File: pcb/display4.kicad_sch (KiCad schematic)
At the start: 20 parts, among them Q13 DMG2301L, Q14 DMG2301L, Q15 DMG2301L, Q16 DMG2301L, U5 TPIC6C596

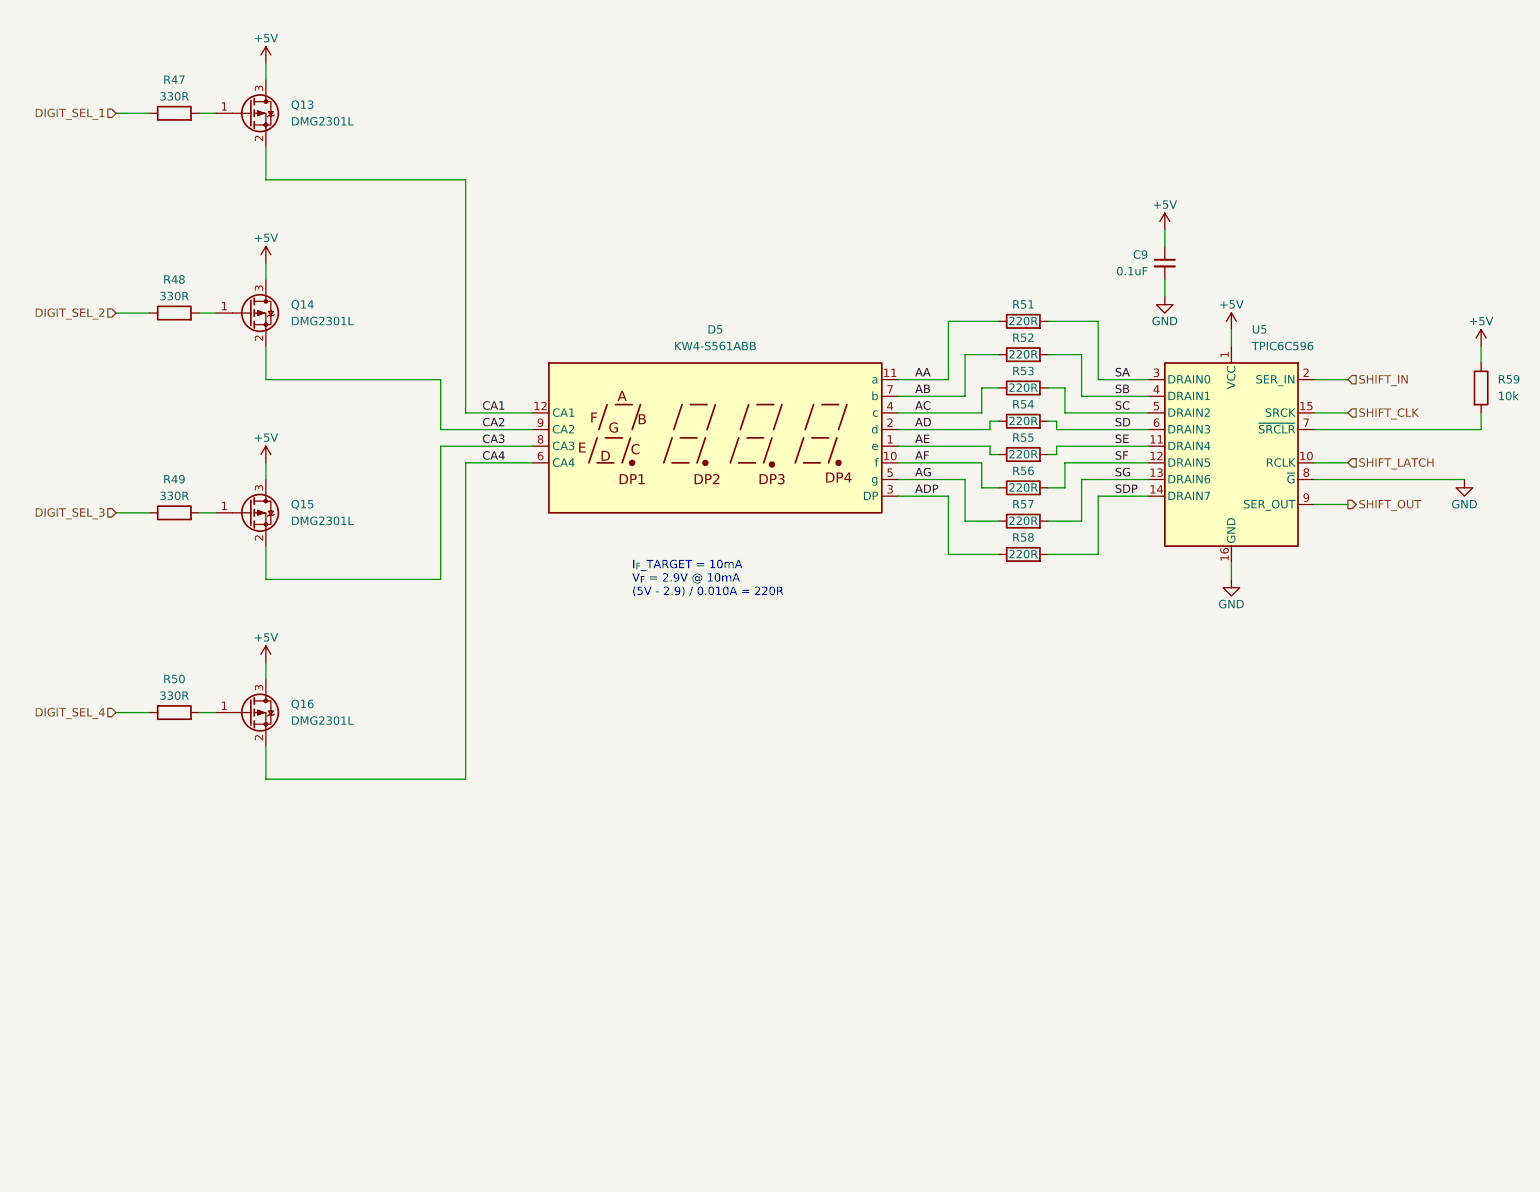
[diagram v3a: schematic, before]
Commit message: start to route display traces
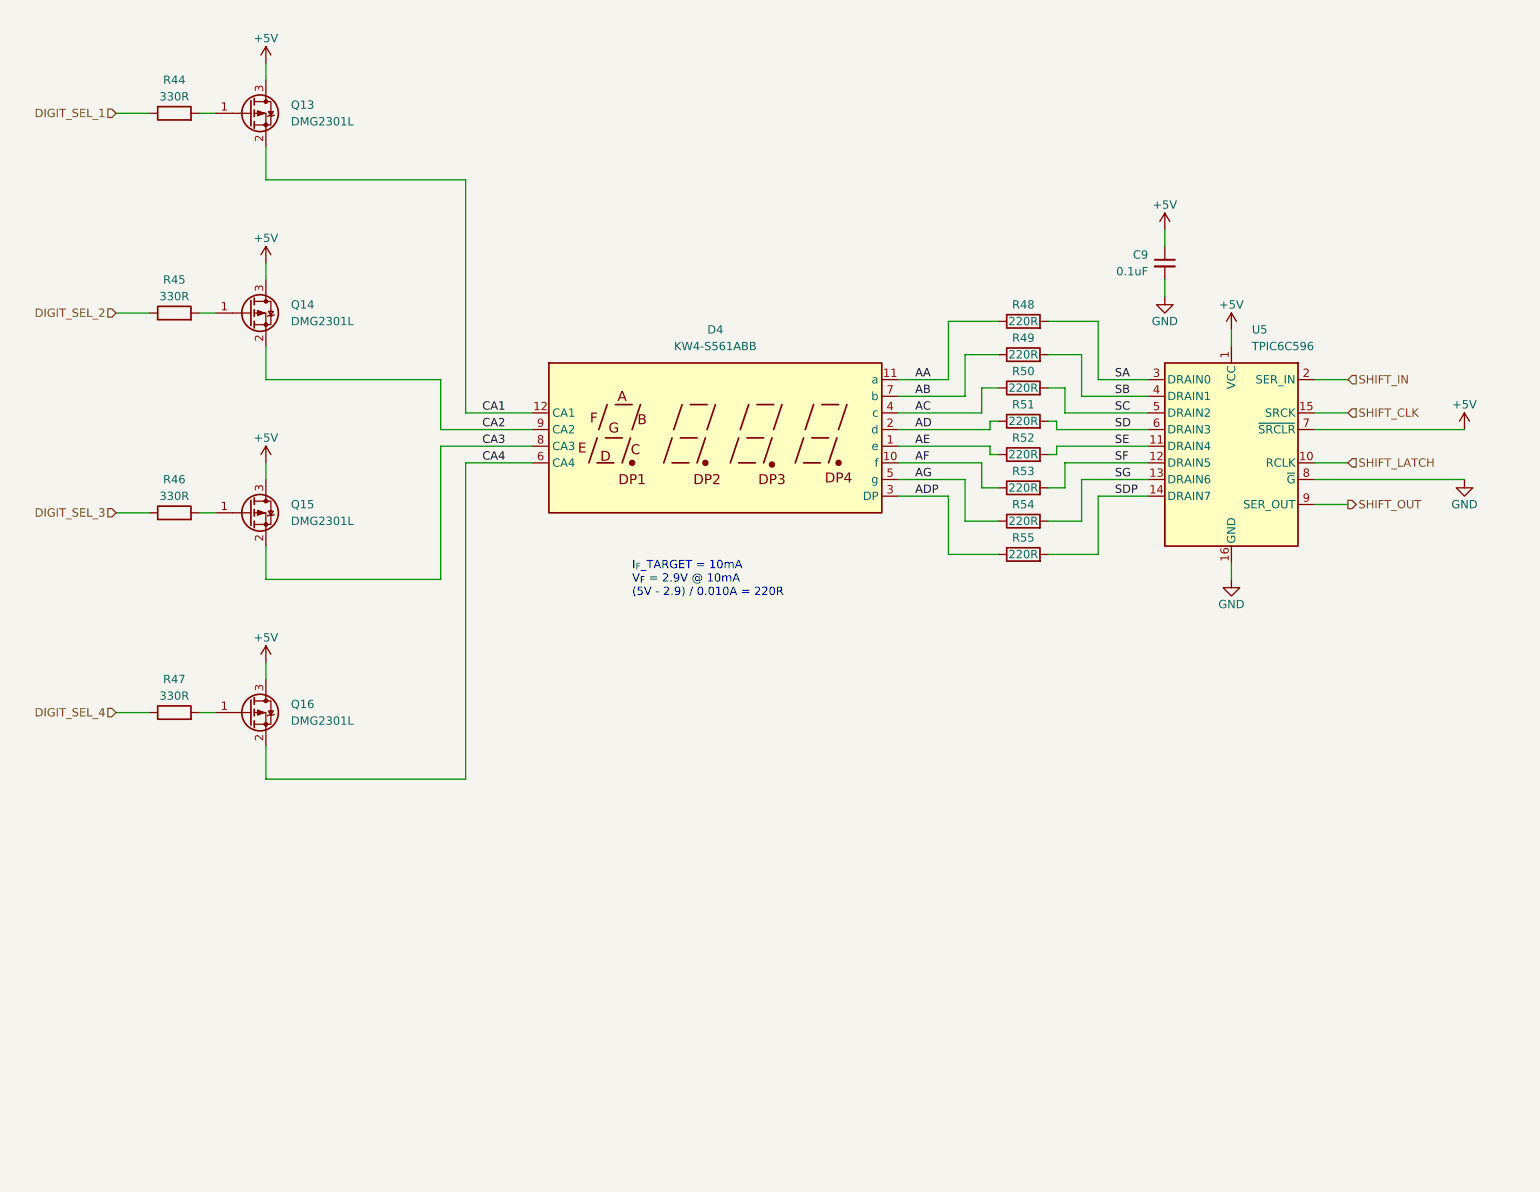
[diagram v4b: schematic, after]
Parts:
- removed R59: 10k, Resistor_SMD:R_0805_2012Metric_Pad1.20x1.40mm_HandSolder, symbol Device:R
- renumbered D5 to D4, R47 to R44, R48 to R45, R49 to R46, R50 to R47, R51 to R48, R52 to R49, R53 to R50, R54 to R51, R55 to R52, R56 to R53, R57 to R54, R58 to R55
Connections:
- net +5V: now also U5.7 (~{SRCLR})

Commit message: continue layout. improve 3d model
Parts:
- D4: footprint mtg_life_counter:KW4-S561xxB_SMD -> mtg_life_counter:KW4-S561xBB_SMD
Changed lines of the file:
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@@
 			)
 		)
-		(property "Footprint" "mtg_life_counter:KW4-S561xxB_SMD"
+		(property "Footprint" "mtg_life_counter:KW4-S561xBB_SMD"
 			(at 132.08 95.25 0)
 			(effects

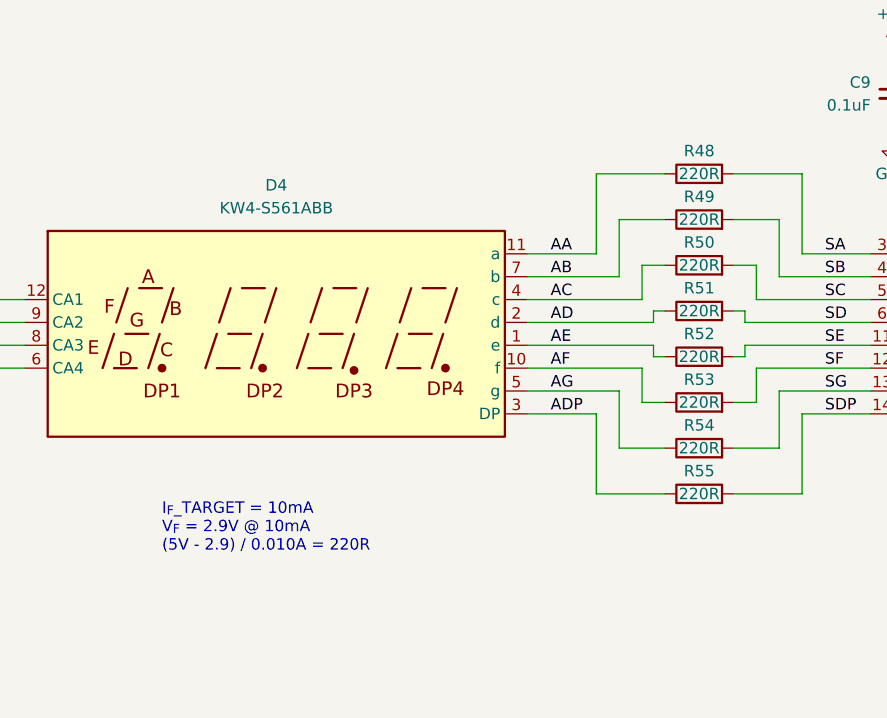
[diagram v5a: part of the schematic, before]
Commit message: continue layout. update leds for KD4 led modules
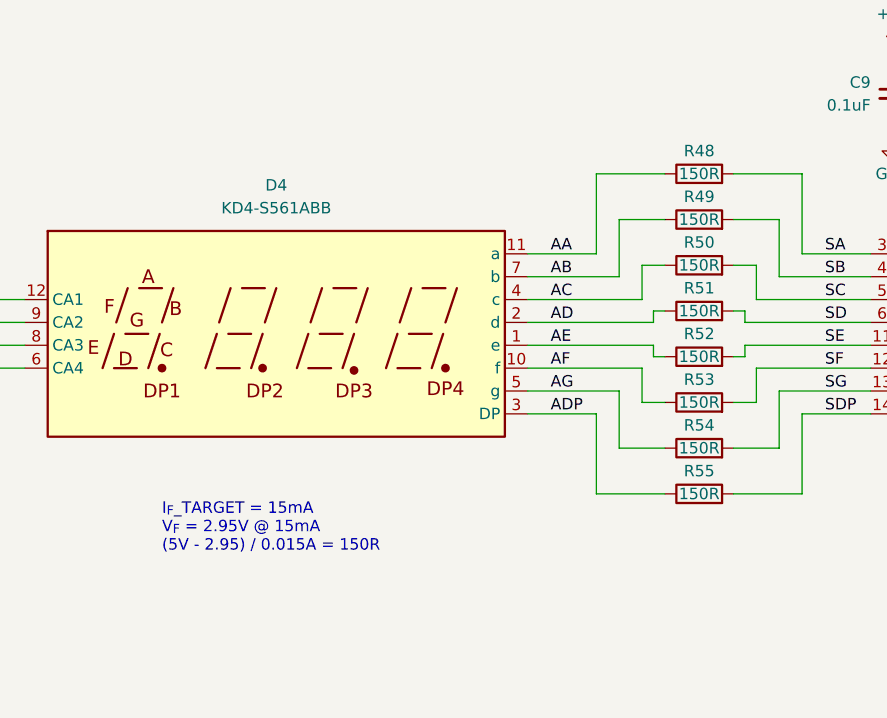
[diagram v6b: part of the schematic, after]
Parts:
- D4: value KW4-S561ABB -> KD4-S561ABB; footprint mtg_life_counter:KW4-S561xBB_SMD -> mtg_life_counter:KD4-S561xxB_SMD_Slim
- R48, R49, R50, R51, R52, R53, R54, R55: value 220R -> 150R
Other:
- note added: "I_{F}_TARGET = 15mA V_{F} = 2.95V @ 15mA (5V - 2.95) / 0.015A = 150R"
- note removed: "I_{F}_TARGET = 10mA V_{F} = 2.9V @ 10mA (5V - 2.9) / 0.010A = 220R"
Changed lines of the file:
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@@
 		(company "Max Proskauer")
 	)
-	(text "I_{F}_TARGET = 10mA\nV_{F} = 2.9V @ 10mA\n(5V - 2.9) / 0.010A = 220R"
+	(text "I_{F}_TARGET = 15mA\nV_{F} = 2.95V @ 15mA\n(5V - 2.95) / 0.015A = 150R"
 		(exclude_from_sim no)
 		(at 119.38 104.14 0)
@@
 			)
 		)
-		(property "Value" "220R"
+		(property "Value" "150R"
 			(at 179.07 80.01 90)
 			(effects
@@
 			)
 		)
-		(property "Value" "220R"
+		(property "Value" "150R"
 			(at 179.07 100.33 90)
 			(effects
@@
 			)
 		)
-		(property "Value" "KW4-S561ABB"
+		(property "Value" "KD4-S561ABB"
 			(at 132.08 68.58 0)
 			(effects
@@
 			)
 		)
-		(property "Footprint" "mtg_life_counter:KW4-S561xBB_SMD"
+		(property "Footprint" "mtg_life_counter:KD4-S561xxB_SMD_Slim"
 			(at 132.08 95.25 0)
 			(effects
@@
 			)
 		)
-		(property "Value" "220R"
+		(property "Value" "150R"
 			(at 179.07 74.93 90)
 			(effects
@@
 			)
 		)
-		(property "Value" "220R"
+		(property "Value" "150R"
 			(at 179.07 95.25 90)
 			(effects
@@
 			)
 		)
-		(property "Value" "220R"
+		(property "Value" "150R"
 			(at 179.07 64.77 90)
 			(effects
@@
 			)
 		)
-		(property "Value" "220R"
+		(property "Value" "150R"
 			(at 179.07 85.09 90)
 			(effects
@@
 			)
 		)
-		(property "Value" "220R"
+		(property "Value" "150R"
 			(at 179.07 69.85 90)
 			(effects
@@
 			)
 		)
-		(property "Value" "220R"
+		(property "Value" "150R"
 			(at 179.07 90.17 90)
 			(effects
